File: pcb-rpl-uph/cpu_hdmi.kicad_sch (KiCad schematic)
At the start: 1 part, among them U5 RPL_UPH_FCBGA1744

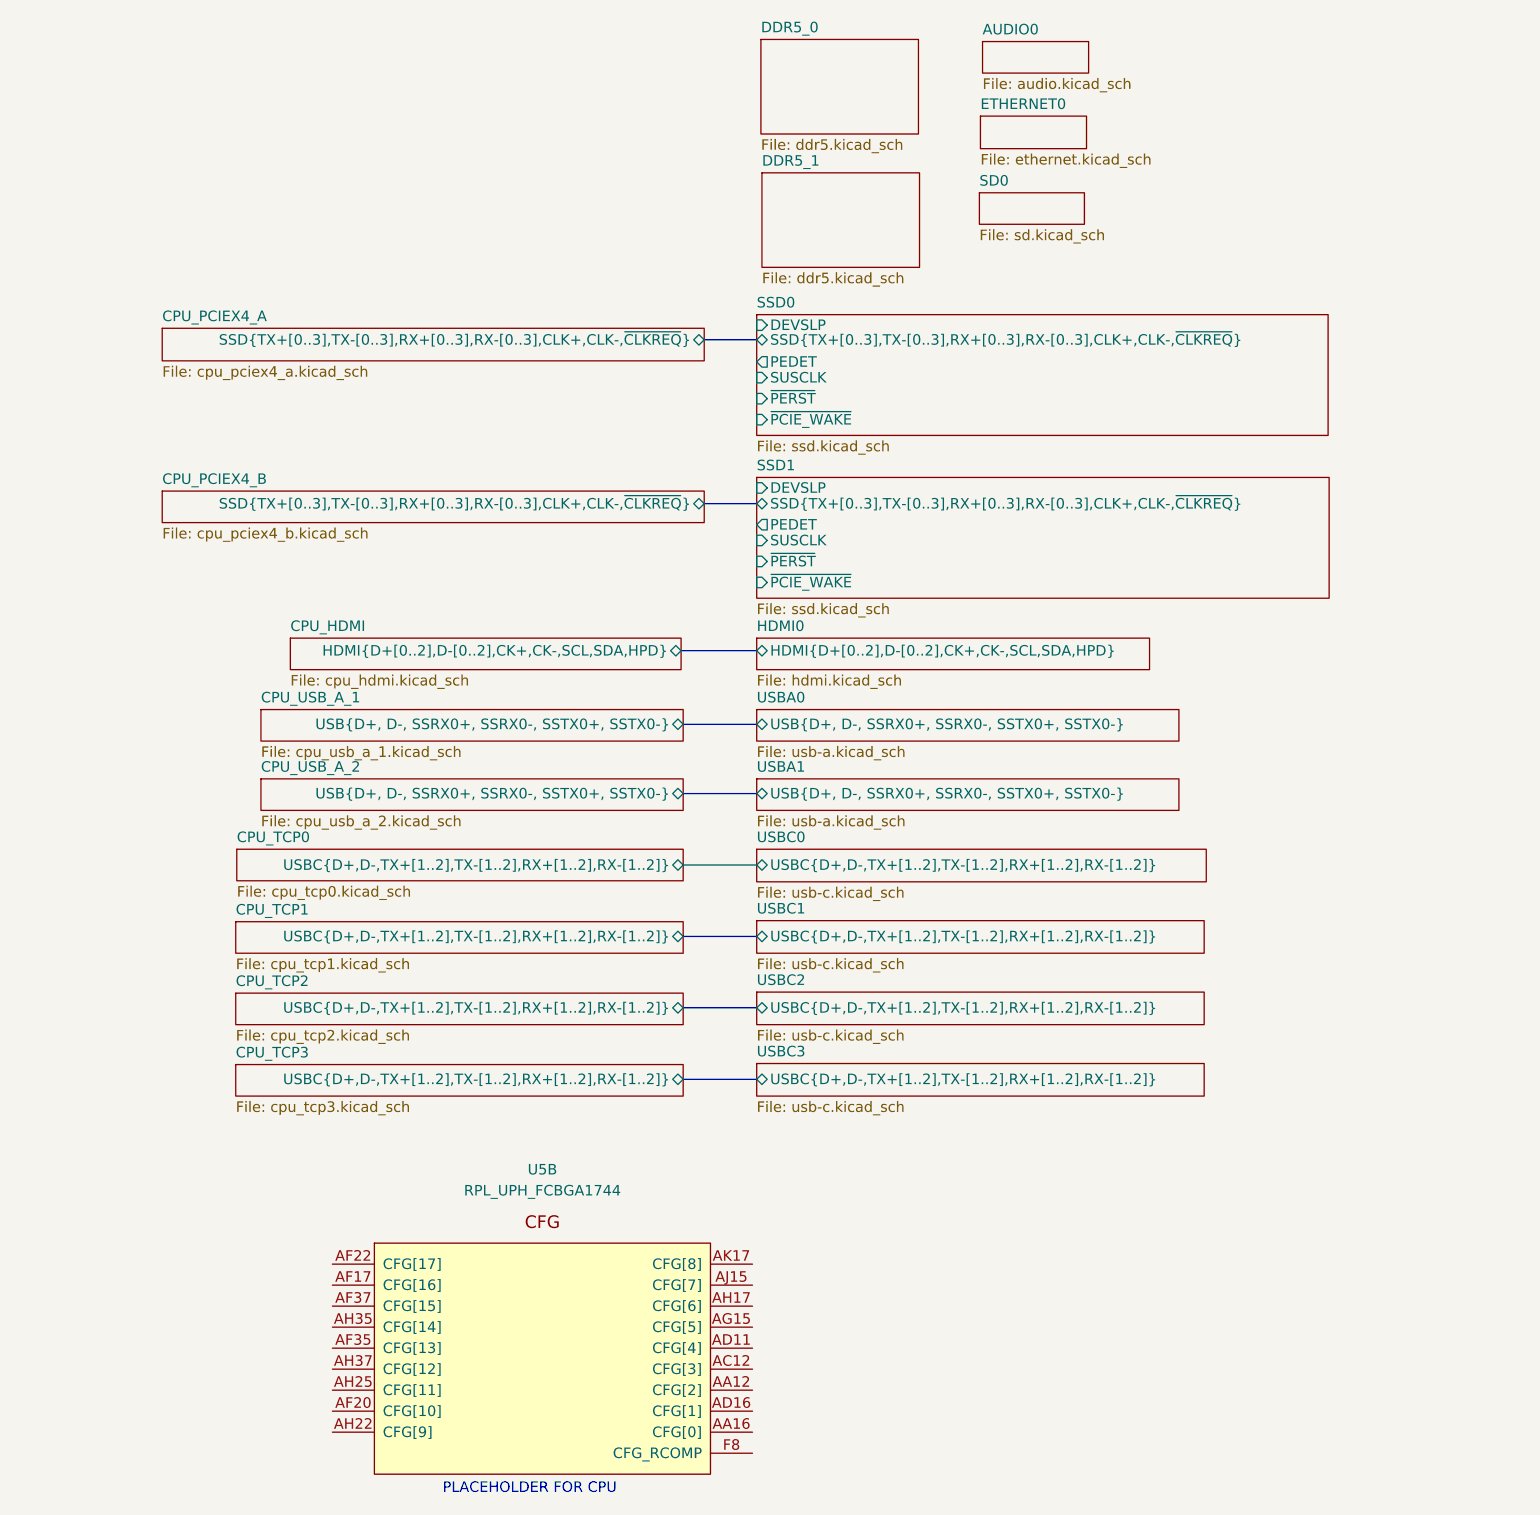
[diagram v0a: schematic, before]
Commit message: Connect USB-A and USB-C data
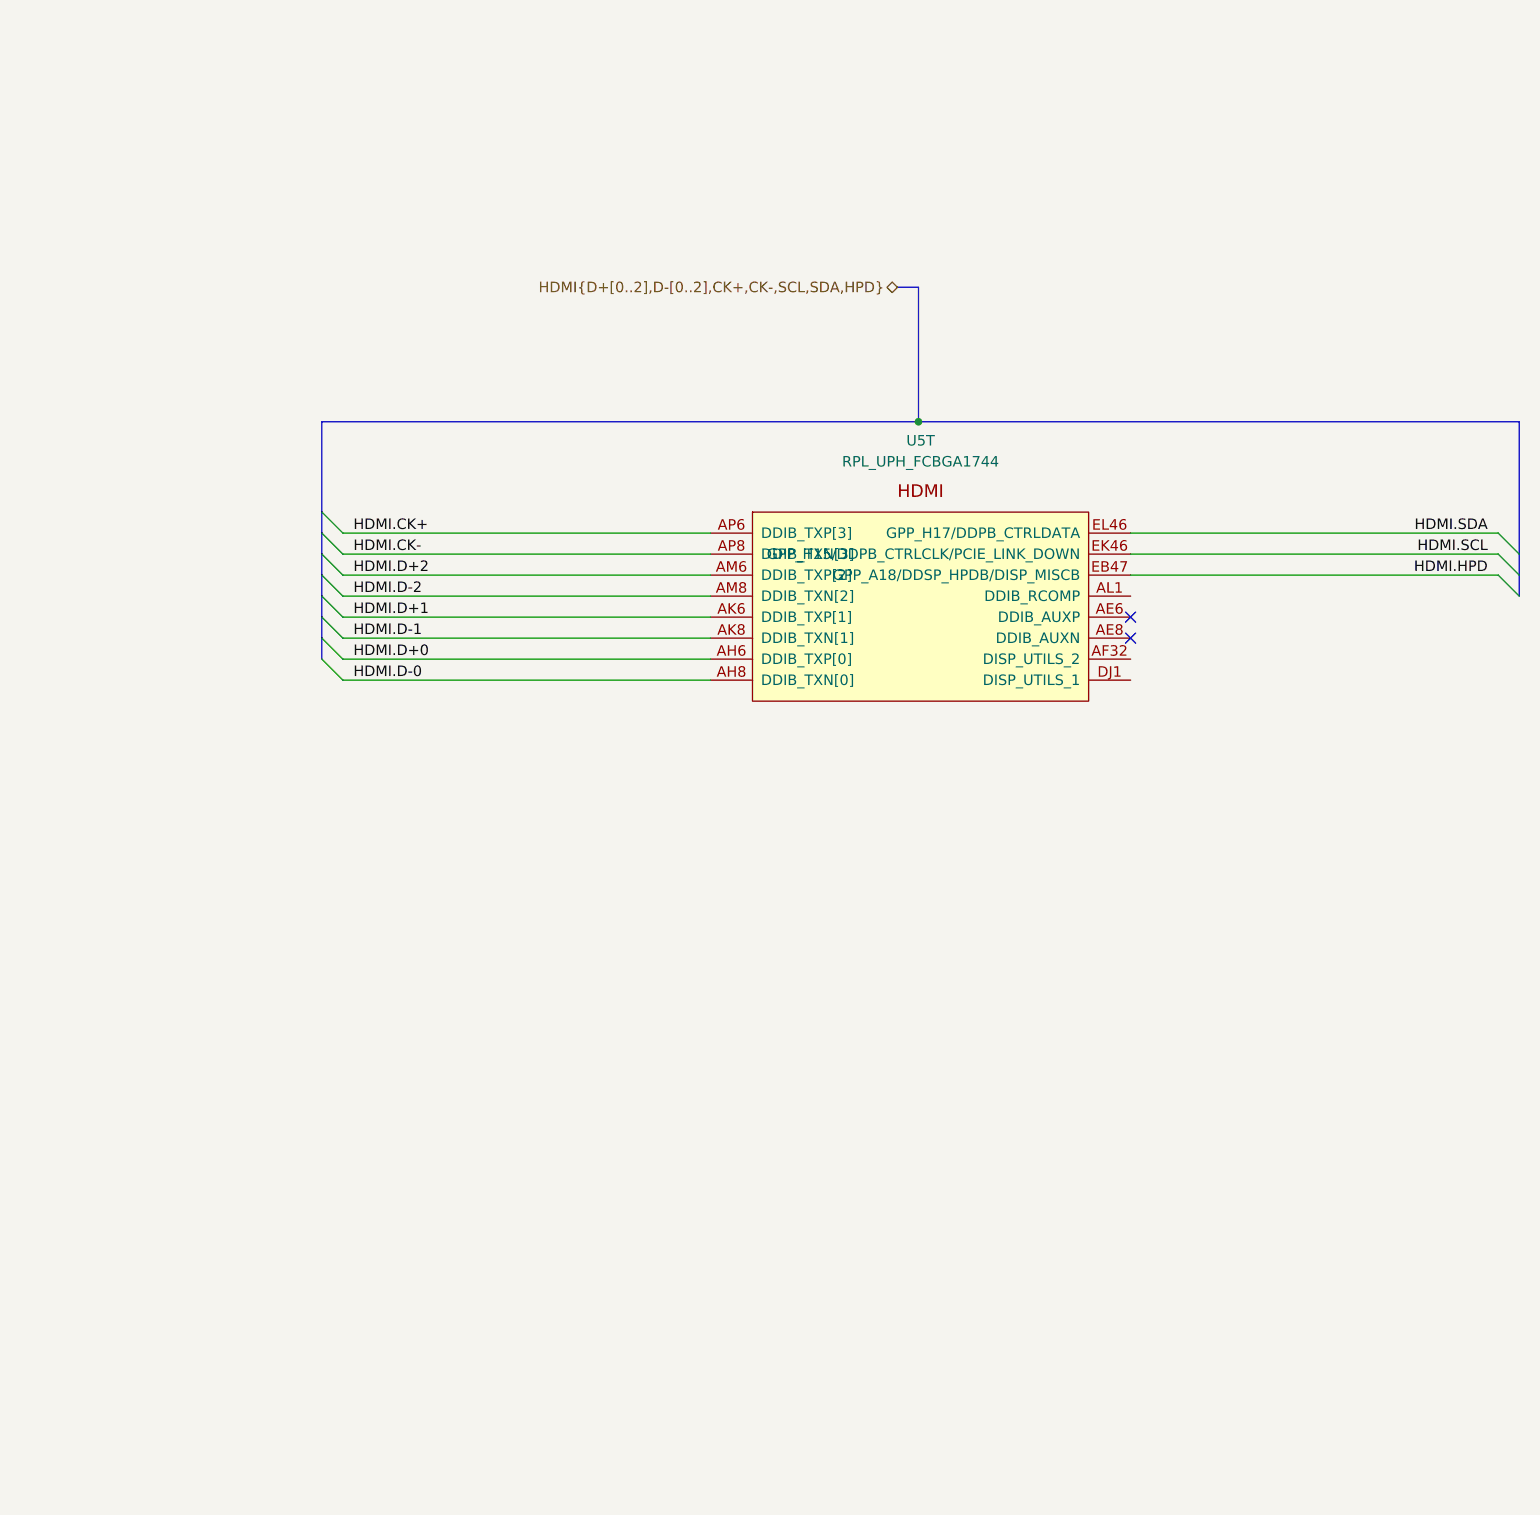
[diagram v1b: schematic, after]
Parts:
- removed U5: RPL_UPH_FCBGA1744, local:RPL_UPH_FCBGA1744, symbol local:RPL_UPH_FCBGA1744
- added U5: RPL_UPH_FCBGA1744, symbol local:RPL_UPH_FCBGA1744
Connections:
- new net HDMI.CK+: U5.AP6 (DDIB_TXP[3])
- new net HDMI.CK-: U5.AP8 (DDIB_TXN[3])
- new net HDMI.D+0: U5.AH6 (DDIB_TXP[0])
- new net HDMI.D+1: U5.AK6 (DDIB_TXP[1])
- new net HDMI.D+2: U5.AM6 (DDIB_TXP[2])
- new net HDMI.D-0: U5.AH8 (DDIB_TXN[0])
- new net HDMI.D-1: U5.AK8 (DDIB_TXN[1])
- new net HDMI.D-2: U5.AM8 (DDIB_TXN[2])
- new net HDMI.HPD: U5.EB47 (GPP_A18/DDSP_HPDB/DISP_MISCB)
- new net HDMI.SCL: U5.EK46 (GPP_H15/DDPB_CTRLCLK/PCIE_LINK_DOWN)
- new net HDMI.SDA: U5.EL46 (GPP_H17/DDPB_CTRLDATA)
- no-connect marks 0 -> 2
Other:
- removed sheet AUDIO0
- removed sheet CPU_HDMI
- removed sheet CPU_PCIEX4_A
- removed sheet CPU_PCIEX4_B
- removed sheet CPU_TCP0
- removed sheet CPU_TCP1
- removed sheet CPU_TCP2
- removed sheet CPU_TCP3
- removed sheet CPU_USB_A_1
- removed sheet CPU_USB_A_2
- removed sheet DDR5_0
- removed sheet DDR5_1
- removed sheet ETHERNET0
- removed sheet HDMI0
- removed sheet SD0
- removed sheet SSD0
- removed sheet SSD1
- removed sheet USBA0
- removed sheet USBA1
- removed sheet USBC0
- removed sheet USBC1
- removed sheet USBC2
- removed sheet USBC3
- note removed: "PLACEHOLDER FOR CPU"

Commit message: add display connector
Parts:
- added R1: 150, local:R_0201_0603Metric, symbol Device:R
- U5: footprint (none) -> local:RPL_UPH_FCBGA1744
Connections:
- net DDIB__RCOMP: now reaches U5.AL1 (DDIB_RCOMP)
- net DDIB__RCOMP: now also R1.1
- new net GND: R1.2
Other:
- moved on the sheet: U5T
